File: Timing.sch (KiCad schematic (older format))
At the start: 5 parts, among them U15 74HC4040, U16 74HC4040, U17 GAL22V10

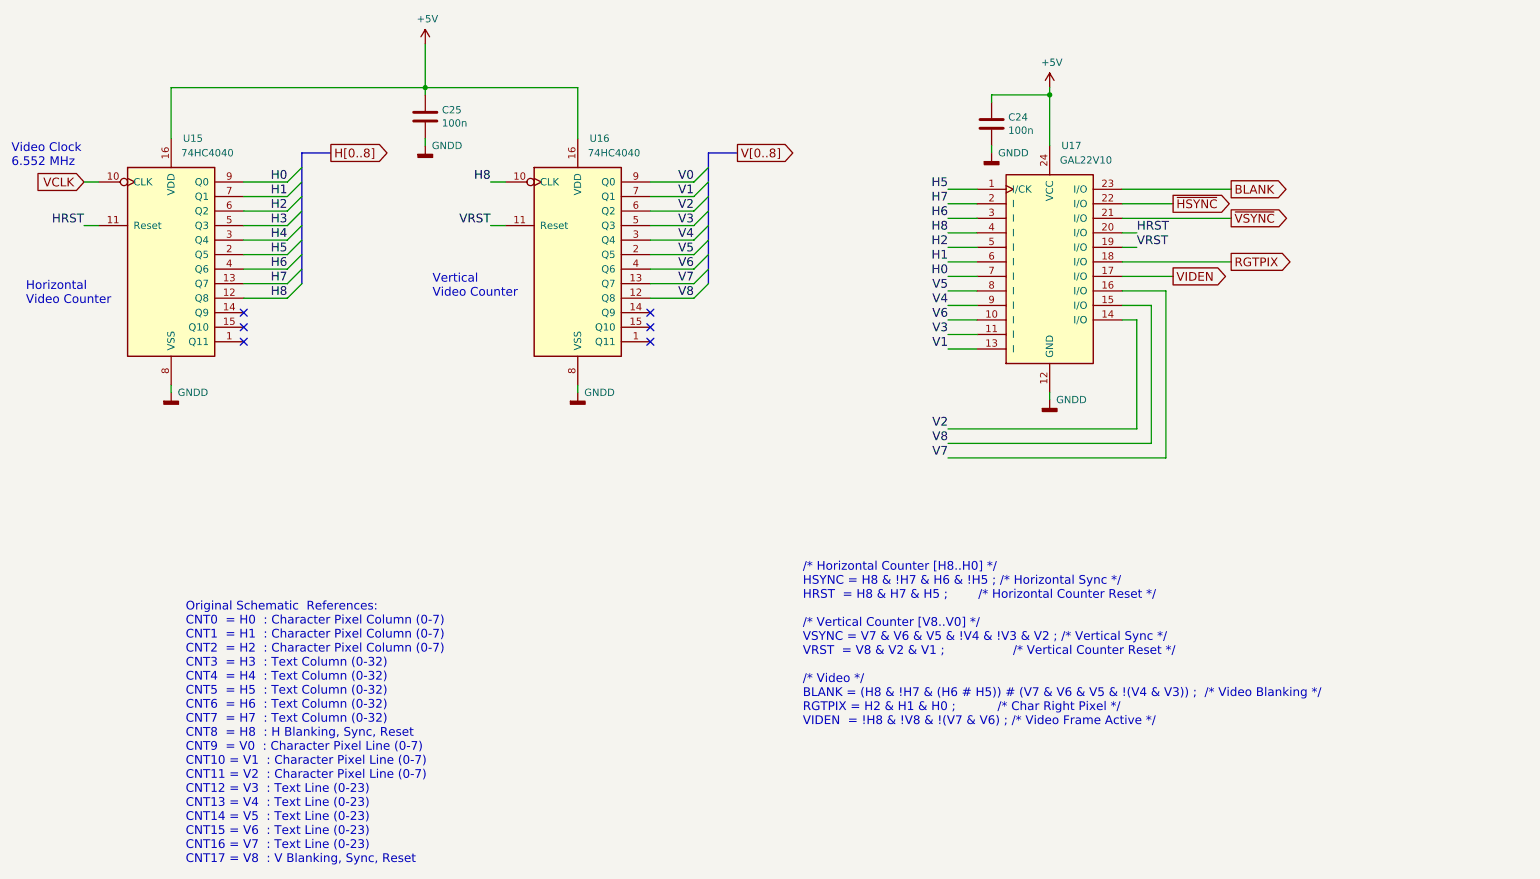
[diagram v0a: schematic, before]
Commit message: Inverted video option
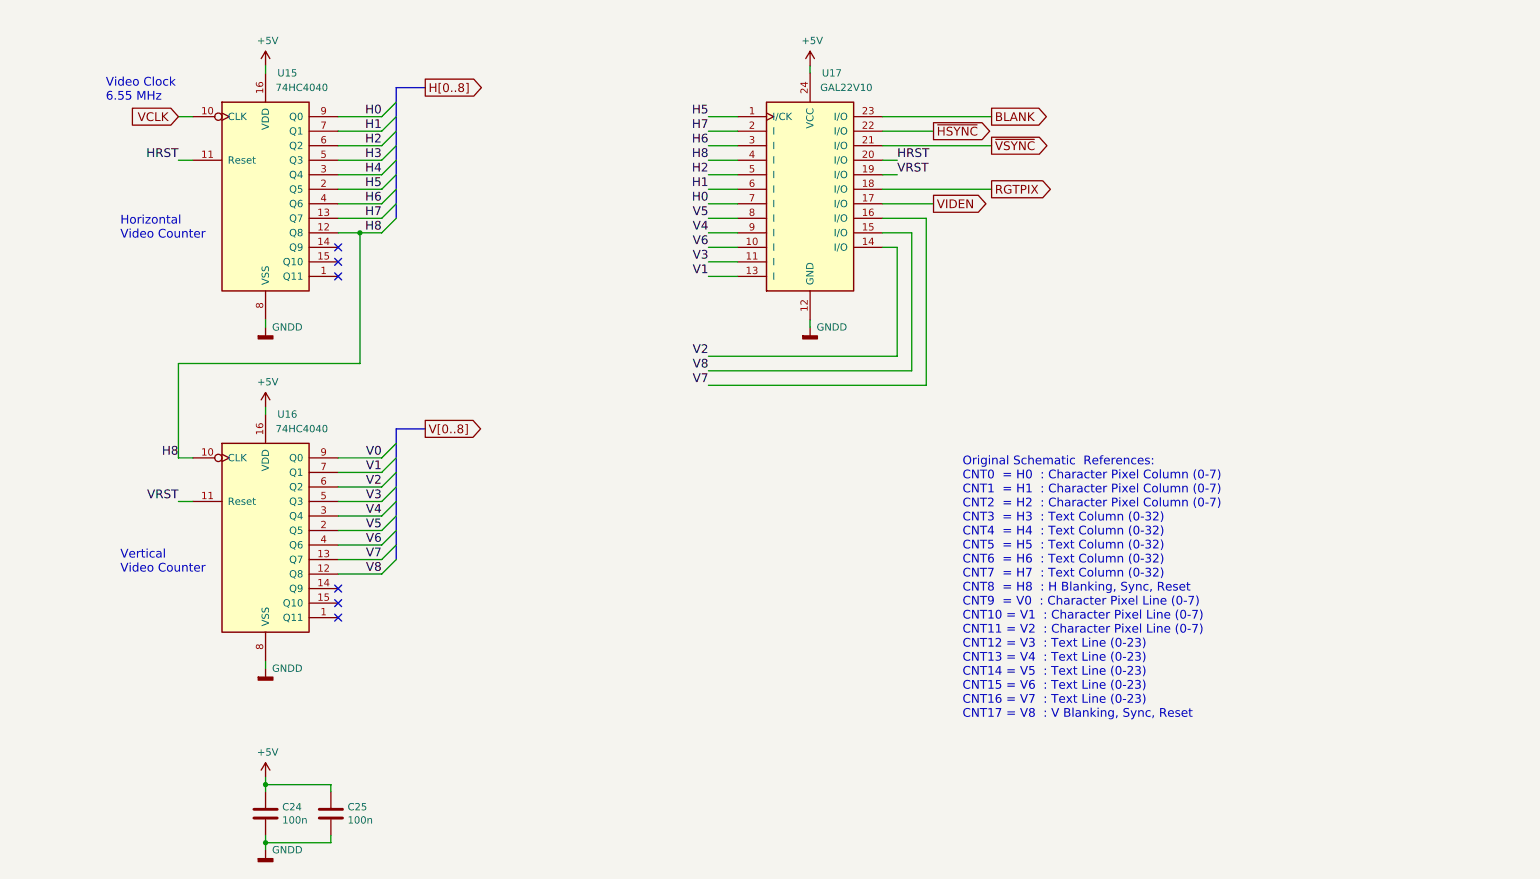
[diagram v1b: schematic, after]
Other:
- note added: "Video Clock\n6.55 MHz"
- note removed: "/* Horizontal Counter [H8..H0] */\nHSYNC = H8 & !H7 & H6 & !H5 ; /* Horizontal Sync */\nHRST = H8 & H7 & H5 ; /* Horizontal Counter Reset */\n\n/* Vertical Counter [V8..V0] */\nVSYNC = V7 & V6 & V5 & !V4 & !V3 & V2 ; /* Vertical Sync */\nVRST = V8 & V2 & V1 ; /* Vertical Counter Reset */\n\n/* Video */\nBLANK = (H8 & !H7 & (H6 # H5)) # (V7 & V6 & V5 & !(V4 & V3)) ; /* Video Blanking */\nRGTPIX = 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"
- note removed: "Video Clock\n6.552 MHz"
- moved on the sheet: C24, C25, U15, U16, U17

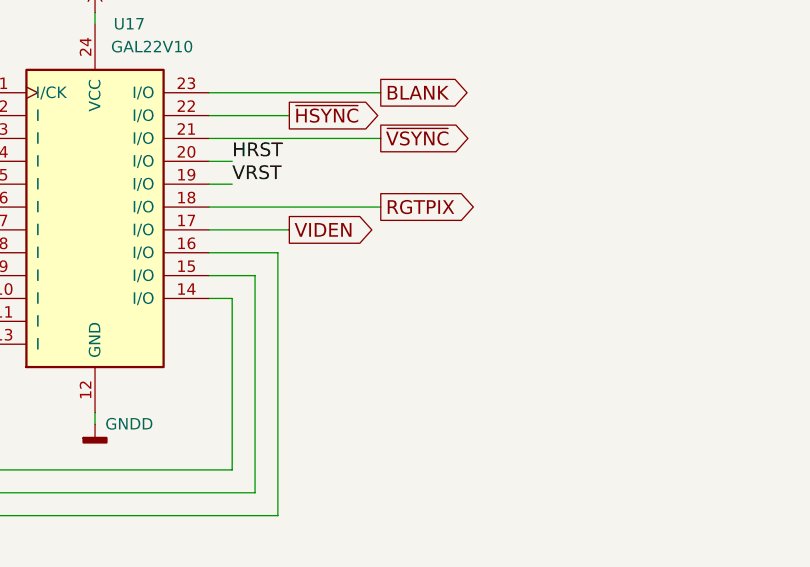
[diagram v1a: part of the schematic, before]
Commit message: Removing video glitches
Glitches occurs on VIDEN and WAIT lines due to the use of asynchronous counters 74HC4040 (the same occurs when using the 74LS393). Those gliteches are usually controlled by a filtering capacitor in the WAIT line. Here a capacitor was also included at the VIDEN line before WAIT signal generation.
Those glitches can be seen as image interference on screen while the CPU are accessing video memory.
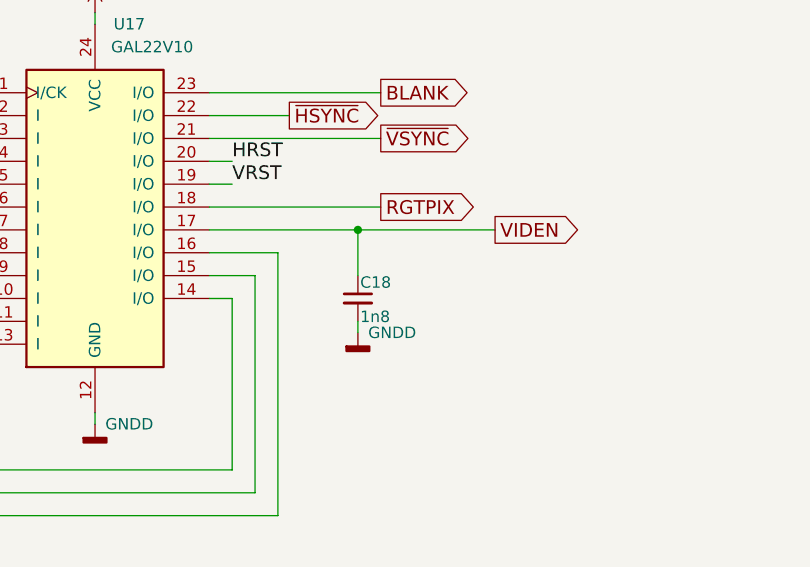
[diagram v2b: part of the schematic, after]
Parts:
- added C18: 1n8, Capacitors_SMD:C_0805_HandSoldering, symbol Device:C_Small
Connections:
- net GNDD: now also C18.2
- net VIDEN: now also C18.1
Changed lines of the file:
@@
 Text GLabel 8250 2650 2    60   Output ~ 0
 RGTPIX
-Text GLabel 7850 2750 2    60   Output ~ 0
+Text GLabel 8750 2750 2    60   Output ~ 0
 VIDEN
 Wire Wire Line
-	7500 2750 7850 2750
+	7500 2750 8150 2750
 Text GLabel 7850 2250 2    60   Output ~ 0
 ~HSYNC
@@
 Wire Wire Line
 	3900 2950 4050 2950
+Wire Wire Line
+	8150 2950 8150 2750
+Connection ~ 8150 2750
+Wire Wire Line
+	8150 2750 8750 2750
+Wire Wire Line
+	8150 3150 8150 3200
+$Comp
+L power:GNDD #PWR05
+U 1 1 5EC5A88F
+P 8150 3200
+F 0 "#PWR05" H 8150 2950 50  0001 C CNN
+F 1 "GNDD" H 8300 3200 50  0000 C CNN
+F 2 "" H 8150 3200 50  0001 C CNN
+F 3 "" H 8150 3200 50  0001 C CNN
+	1    8150 3200
+	1    0    0    -1
+$EndComp
+$Comp
+L Device:C_Small C?
+U 1 1 5EC5E42D
+P 8150 3050
+AR Path="/5699553D/5EC5E42D" Ref="C?"  Part="1"
+AR Path="/5EC5E42D" Ref="C?"  Part="1"
+AR Path="/56995FEC/5EC5E42D" Ref="C18"  Part="1"
+F 0 "C18" H 8160 3120 50  0000 L CNN
+F 1 "1n8" H 8160 2970 50  0000 L CNN
+F 2 "Capacitors_SMD:C_0805_HandSoldering" H 8150 3050 50  0001 C CNN
+F 3 "" H 8150 3050 50  0000 C CNN
+	1    8150 3050
+	1    0    0    -1
+$EndComp
 Wire Bus Line
 	4150 1950 4150 2850

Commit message: Video improvement (#6)
* Preparing for expansion

* PLD update for expansion

* PLD update
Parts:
- C18: footprint Capacitors_SMD:C_0805_HandSoldering -> Capacitor_SMD:C_0805_2012Metric_Pad1.15x1.40mm_HandSolder
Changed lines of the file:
@@
 Text Label 7600 2450 0    60   ~ 0
 HRST
-Text GLabel 8250 2350 2    60   Output ~ 0
+Text GLabel 8400 2450 2    60   Output ~ 0
 ~VSYNC
 $Comp
@@
 Wire Wire Line
 	7800 4000 6300 4000
-Text GLabel 8250 2150 2    60   Output ~ 0
+Text GLabel 8400 2100 2    60   Output ~ 0
 BLANK
 Wire Wire Line
-	7500 2250 7850 2250
+	7500 2250 8400 2250
 Wire Wire Line
 	3250 4150 3250 4200
 Wire Wire Line
 	7500 2650 8250 2650
-Text GLabel 8250 2650 2    60   Output ~ 0
+Text GLabel 8400 2600 2    60   Output ~ 0
 RGTPIX
-Text GLabel 8750 2750 2    60   Output ~ 0
+Text GLabel 8400 2750 2    60   Output ~ 0
 VIDEN
 Wire Wire Line
 	7500 2750 8150 2750
-Text GLabel 7850 2250 2    60   Output ~ 0
+Text GLabel 8400 2250 2    60   Output ~ 0
 ~HSYNC
 Text Notes 8050 6300 0    60   ~ 0
@@
 Connection ~ 8150 2750
 Wire Wire Line
-	8150 2750 8750 2750
+	8150 2750 8400 2750
 Wire Wire Line
 	8150 3150 8150 3200
@@
 F 0 "C18" H 8160 3120 50  0000 L CNN
 F 1 "1n8" H 8160 2970 50  0000 L CNN
-F 2 "Capacitors_SMD:C_0805_HandSoldering" H 8150 3050 50  0001 C CNN
+F 2 "Capacitor_SMD:C_0805_2012Metric_Pad1.15x1.40mm_HandSolder" H 8150 3050 50  0001 C CNN
 F 3 "" H 8150 3050 50  0000 C CNN
 	1    8150 3050
 	1    0    0    -1
 $EndComp
+Wire Wire Line
+	8250 2650 8250 2600
+Wire Wire Line
+	8250 2600 8400 2600
+Wire Wire Line
+	8250 2350 8250 2450
+Wire Wire Line
+	8250 2450 8400 2450
+Wire Wire Line
+	8250 2150 8250 2100
+Wire Wire Line
+	8250 2100 8400 2100
 Wire Bus Line
 	4150 1950 4150 2850
